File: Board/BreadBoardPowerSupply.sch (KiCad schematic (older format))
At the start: 6 parts, among them CON1 BARREL_JACK, U1 7805

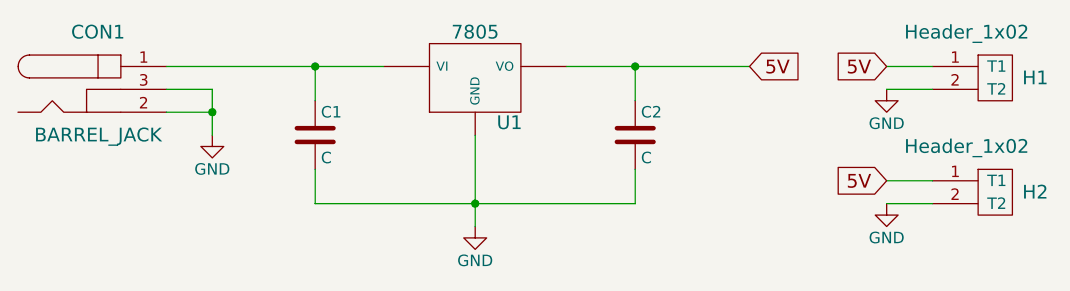
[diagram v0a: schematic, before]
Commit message: Update schematics (added polarised capacitors)
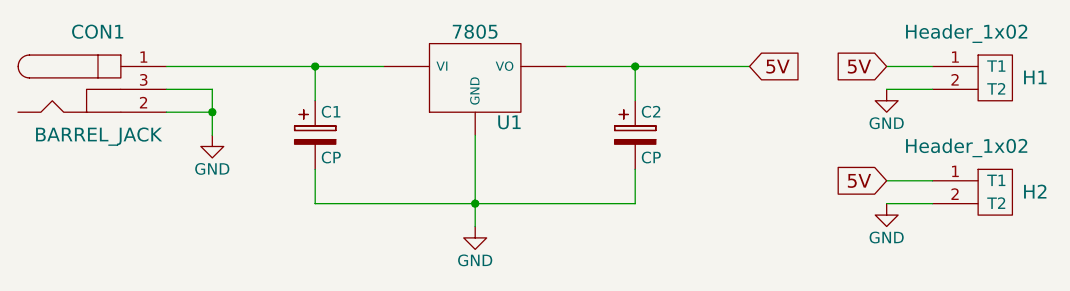
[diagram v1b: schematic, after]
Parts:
- removed C1: C, Capacitors_ThroughHole:C_Radial_D10_L13_P5, symbol C
- removed C2: C, Capacitors_ThroughHole:C_Radial_D5_L6_P2.5, symbol C
- added C1: CP, Capacitors_Elko_ThroughHole:Elko_vert_20x10mm_RM5, symbol CP
- added C2: CP, Capacitors_Elko_ThroughHole:Elko_vert_11x5mm_RM2.5, symbol CP
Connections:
- net 5V: now also C2.1
- net GND: now also C1.2, C2.2
- net at CON1.1, U1.VI: now also C1.1
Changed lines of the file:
@@
-$EndComp
-$Comp
-L C C1
-U 1 1 55D1EDF9
-P 3500 2500
-F 0 "C1" H 3525 2600 50  0000 L CNN
-F 1 "C" H 3525 2400 50  0000 L CNN
-F 2 "Capacitors_ThroughHole:C_Radial_D10_L13_P5" H 3538 2350 30  0001 C CNN
-F 3 "" H 3500 2500 60  0000 C CNN
-	1    3500 2500
-	1    0    0    -1
-$EndComp
-$Comp
-L C C2
-U 1 1 55D1EE1A
-P 4900 2500
-F 0 "C2" H 4925 2600 50  0000 L CNN
-F 1 "C" H 4925 2400 50  0000 L CNN
-F 2 "Capacitors_ThroughHole:C_Radial_D5_L6_P2.5" H 4938 2350 30  0001 C CNN
-F 3 "" H 4900 2500 60  0000 C CNN
-	1    4900 2500
-	1    0    0    -1
 $EndComp
 $Comp
@@
 	6000 2700 6200 2700
 $Comp
-L GND #PWR?
+L GND #PWR04
 U 1 1 55D1F812
 P 6000 2800
-F 0 "#PWR?" H 6000 2550 50  0001 C CNN
+F 0 "#PWR04" H 6000 2550 50  0001 C CNN
 F 1 "GND" H 6000 2650 50  0000 C CNN
 F 2 "" H 6000 2800 60  0000 C CNN
@@
 Wire Wire Line
 	6000 2800 6200 2800
+$Comp
+L CP C1
+U 1 1 55DAD95D
+P 3500 2500
+F 0 "C1" H 3525 2600 50  0000 L CNN
+F 1 "CP" H 3525 2400 50  0000 L CNN
+F 2 "Capacitors_Elko_ThroughHole:Elko_vert_20x10mm_RM5" H 3538 2350 30  0001 C CNN
+F 3 "" H 3500 2500 60  0000 C CNN
+	1    3500 2500
+	1    0    0    -1
+$EndComp
+$Comp
+L CP C2
+U 1 1 55DAD9DE
+P 4900 2500
+F 0 "C2" H 4925 2600 50  0000 L CNN
+F 1 "CP" H 4925 2400 50  0000 L CNN
+F 2 "Capacitors_Elko_ThroughHole:Elko_vert_11x5mm_RM2.5" H 4938 2350 30  0001 C CNN
+F 3 "" H 4900 2500 60  0000 C CNN
+	1    4900 2500
+	1    0    0    -1
+$EndComp
 $EndSCHEMATC
